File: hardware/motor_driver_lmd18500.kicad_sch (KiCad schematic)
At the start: 11 parts, among them J6 Screw_Terminal_01x02, J8 Screw_Terminal_01x02, M1 Motor_DC, U2 LMD18200T_NOPB

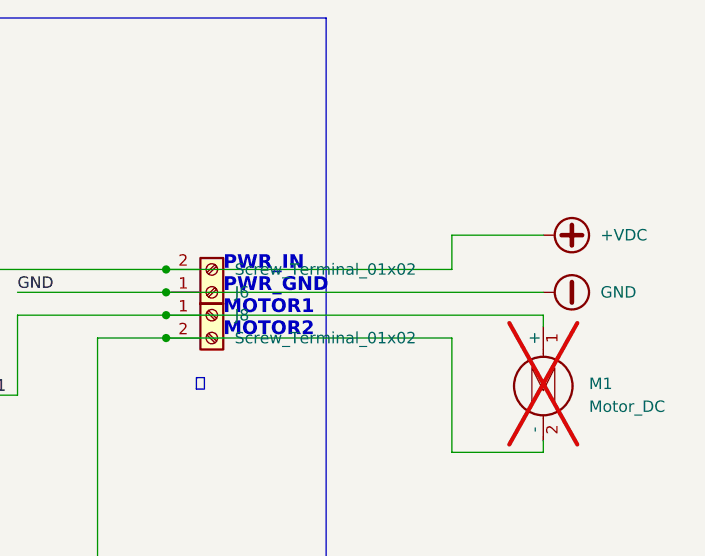
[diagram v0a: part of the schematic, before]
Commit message: pcb almost finalized, needs switch and cap on lower driver shifted to route 12v rail
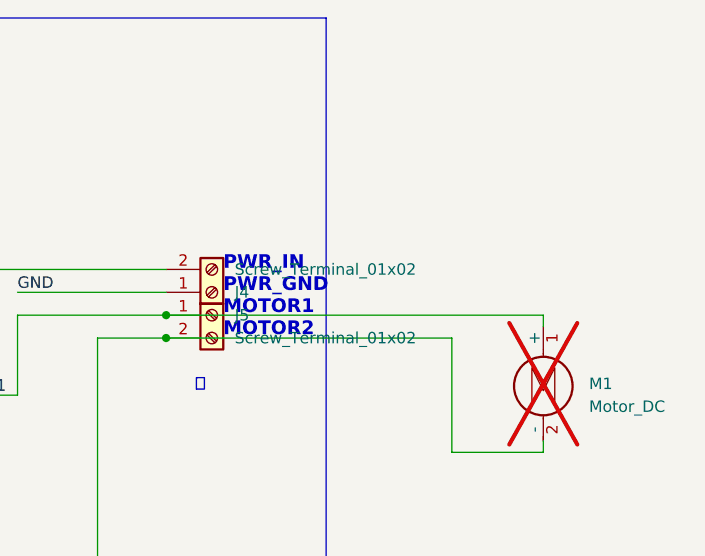
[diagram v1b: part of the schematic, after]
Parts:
- renumbered J6 to J4, J8 to J5

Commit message: review and revise for current template and kmlib
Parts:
- S1: footprint kml-custom:SW_Slide-CK-1101M2S3CQE2 -> KMLib_Switches:SW_Slide-CK-1101M2S3CQE2; symbol kml-custom:1101M2S3CQE2 -> KMLib_Switches:1101M2S3CQE2
- U2: footprint Package_TO_SOT_THT:TO-220-11_P3.4x5.08mm_StaggerOdd_Lead8.45mm_TabDown -> KMLib_IC_THT:TO-220-11_P3.4x5.08mm_StaggerOdd_Lead8.45mm_TabDown
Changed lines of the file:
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@@
 			)
 		)
-		(property "Description" ""
+		(property "Description" "Unpolarized capacitor"
 			(at 147.32 87.63 0)
 			(effects
@@
 	)
 	(symbol
-		(lib_id "kml-custom:1101M2S3CQE2")
+		(lib_id "KMLib_Switches:1101M2S3CQE2")
 		(at 120.65 54.61 0)
 		(unit 1)
@@
 			)
 		)
-		(property "Footprint" "kml-custom:SW_Slide-CK-1101M2S3CQE2"
+		(property "Footprint" "KMLib_Switches:SW_Slide-CK-1101M2S3CQE2"
 			(at 120.65 54.61 0)
 			(effects
@@
 			)
 		)
-		(property "Description" ""
+		(property "Description" "Resistor"
 			(at 68.58 129.54 0)
 			(effects
@@
 			)
 		)
-		(property "Description" ""
+		(property "Description" "Unpolarized capacitor"
 			(at 87.63 59.69 0)
 			(effects
@@
 			)
 		)
-		(property "Description" ""
+		(property "Description" "Unpolarized capacitor"
 			(at 80.01 129.54 0)
 			(effects
@@
 			)
 		)
-		(property "Description" ""
+		(property "Description" "Unpolarized capacitor"
 			(at 147.32 74.93 0)
 			(effects
@@
 			)
 		)
-		(property "Footprint" "Package_TO_SOT_THT:TO-220-11_P3.4x5.08mm_StaggerOdd_Lead8.45mm_TabDown"
+		(property "Footprint" "KMLib_IC_THT:TO-220-11_P3.4x5.08mm_StaggerOdd_Lead8.45mm_TabDown"
 			(at 78.74 120.65 0)
 			(effects
